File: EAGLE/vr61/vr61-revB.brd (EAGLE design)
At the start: 283.8 x 93.3 mm, 191 parts, among them M1 M25C, X1 MICROMOD-2222-C

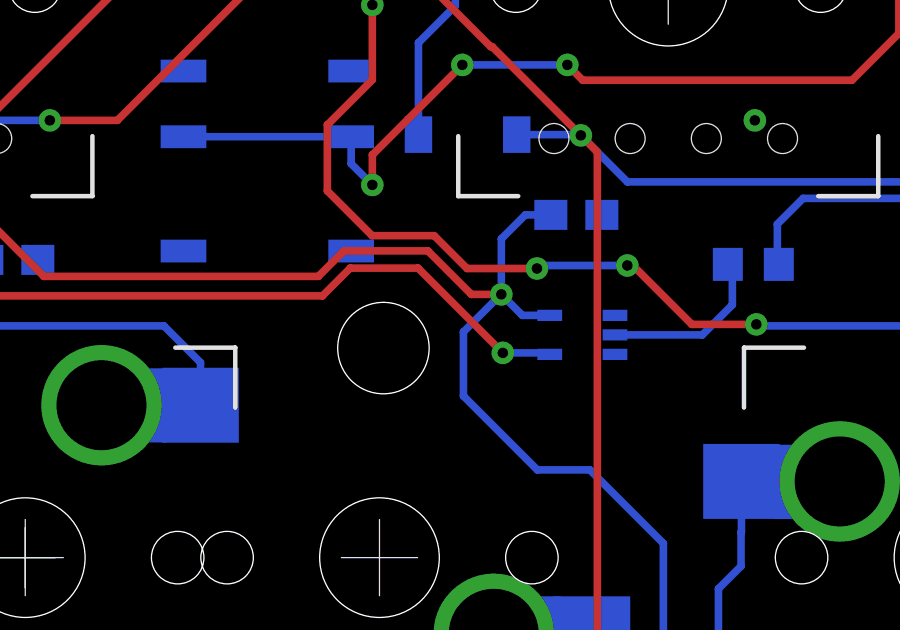
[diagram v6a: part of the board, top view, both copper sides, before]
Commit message: 74AHCT1G125GW
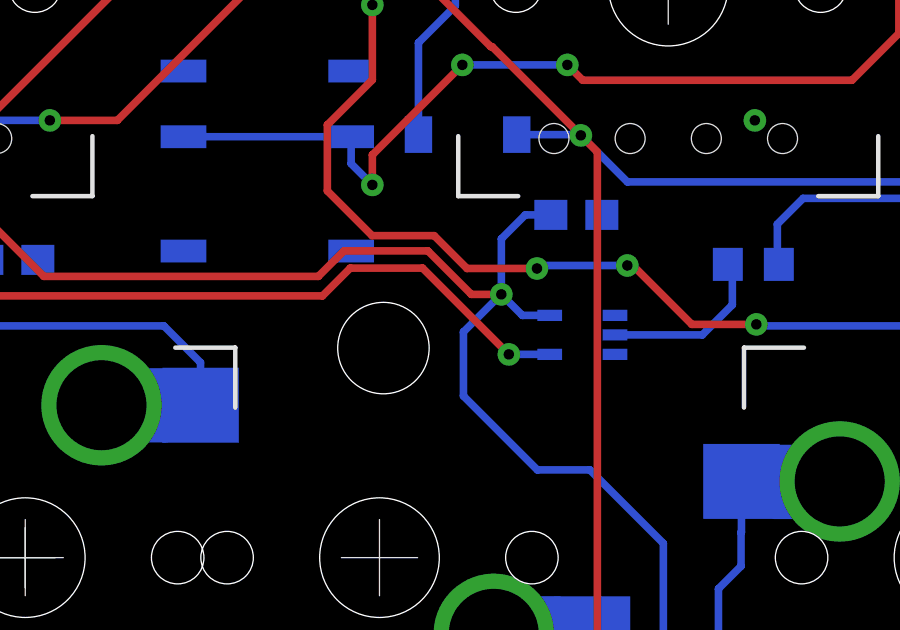
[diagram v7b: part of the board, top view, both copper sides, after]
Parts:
- U$14: value 74AHCT1G125GV -> 74AHCT1G125GW; device ts_keyboards:SC-74A -> ts_keyboards:SC-88A__TSSOP5__SOT353-1
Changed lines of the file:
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@@
 <setting verticaltext="up"/>
 </settings>
-<grid distance="1" unitdist="mm" unit="mm" style="dots" multiple="10" display="yes" altdistance="0.1" altunitdist="mm" altunit="mm"/>
+<grid distance="0.5" unitdist="mm" unit="mm" style="dots" multiple="10" display="yes" altdistance="0.05" altunitdist="mm" altunit="mm"/>
 <layers>
 <layer number="1" name="Top" color="4" fill="1" visible="yes" active="yes"/>
@@
 <element name="S_ENT2" library="ts_keyboards" package="MX-5-PIN-HOTSWAP-PAD-NS" value="MX-5-PIN-HOTSWAP-PADNO-SILK" x="273.844" y="57.15" smashed="yes"/>
 <element name="S_BSLS2" library="ts_keyboards" package="MX-5-PIN-HOTSWAP-PAD-NS" value="MX-5-PIN-HOTSWAP-PADNO-SILK" x="252.413" y="47.625" smashed="yes" rot="R180"/>
-<element name="U$14" library="ts_keyboards" package="SC-74A" value="74AHCT1G125GV" x="40" y="36" smashed="yes" rot="MR270">
-<attribute name="VALUE" x="40" y="34.095" size="0.6096" layer="28" font="vector" ratio="20" rot="MR0" align="bottom-center"/>
-</element>
 <element name="J-HOST" library="SparkFun-Connectors" library_urn="urn:adsk.eagle:library:513" package="1X02" package3d_urn="urn:adsk.eagle:package:38039/1" value="" x="90" y="40.5" smashed="yes" rot="MR90">
 <attribute name="VALUE" x="87.968" y="39.23" size="0.6096" layer="28" font="vector" ratio="20" rot="MR90"/>
@@
 <attribute name="VALUE" x="125.532" y="65.27" size="0.6096" layer="28" font="vector" ratio="20" rot="MR270"/>
 </element>
+<element name="U$14" library="ts_keyboards" package="SC-88A__TSSOP5__SOT353-1" value="74AHCT1G125GW" x="40" y="36" smashed="yes" rot="MR270">
+<attribute name="NAME" x="40" y="37.27" size="0.6096" layer="26" font="vector" ratio="20" rot="MR0" align="bottom-center"/>
+<attribute name="VALUE" x="40" y="34.095" size="0.6096" layer="28" font="vector" ratio="20" rot="MR0" align="bottom-center"/>
+</element>
 </elements>
 <signals>
@@
 <contactref element="J-UBS" pad="GND"/>
 <contactref element="J-UBS" pad="GND2"/>
-<contactref element="C07" pad="2"/>
-<contactref element="C08" pad="2"/>
-<contactref element="C09" pad="2"/>
-<contactref element="C10" pad="2"/>
-<contactref element="C11" pad="2"/>
-<contactref element="C12" pad="2"/>
 <contactref element="C13" pad="2"/>
 <contactref element="M1" pad="4"/>
 <contactref element="R8" pad="1"/>
-<contactref element="U$14" pad="3"/>
-<contactref element="U$14" pad="1"/>
 <via x="70.4" y="54.8" extent="1-16" drill="0.35"/>
 <wire x1="69.65" y1="56.225" x2="69.65" y2="55.25" width="0.254" layer="16"/>
@@
 <via x="115.5" y="89" extent="1-16" drill="0.35"/>
 <via x="71.4" y="58.5" extent="1-16" drill="0.35"/>
+<contactref element="U$14" pad="3"/>
+<contactref element="C07" pad="2"/>
+<contactref element="C08" pad="2"/>
+<contactref element="C09" pad="2"/>
+<contactref element="C10" pad="2"/>
+<contactref element="C11" pad="2"/>
+<contactref element="C12" pad="2"/>
+<contactref element="U$14" pad="1"/>
 </signal>
 <signal name="N$62">
@@
 <wire x1="28.2" y1="75.65" x2="26.55" y2="75.65" width="0.508" layer="16"/>
 <via x="28.2" y="75.65" extent="1-16" drill="0.35"/>
-<contactref element="U$14" pad="6"/>
 <wire x1="45.9012" y1="62.3114" x2="44" y2="62.3114" width="0.508" layer="16"/>
 <via x="44" y="62.3114" extent="1-16" drill="0.35"/>
@@
 <wire x1="66.21026875" y1="59.816" x2="65.32626875" y2="60.7" width="0.254" layer="16"/>
 <wire x1="58.7" y1="60.7" x2="65.32626875" y2="60.7" width="0.254" layer="16"/>
-<wire x1="38.9125" y1="36.65" x2="38" y2="36.65" width="0.254" layer="16"/>
-<wire x1="38" y1="36.65" x2="37.3" y2="37.35" width="0.254" layer="16"/>
 <via x="37.3" y="37.35" extent="1-16" drill="0.35"/>
 <wire x1="37.3" y1="37.35" x2="36.3" y2="37.35" width="0.254" layer="1"/>
@@
 <wire x1="186.85" y1="83.1" x2="186.33" y2="82.58" width="0.254" layer="16"/>
 <wire x1="186.33" y1="82.58" x2="175.62" y2="82.58" width="0.254" layer="16"/>
+<contactref element="U$14" pad="6"/>
+<wire x1="38.9125" y1="36.65" x2="38" y2="36.65" width="0.254" layer="16"/>
+<wire x1="38" y1="36.65" x2="37.3" y2="37.35" width="0.254" layer="16"/>
 </signal>
 <signal name="CC1">
@@
 <signal name="LED1ST">
 <contactref element="R6" pad="1"/>
-<contactref element="U$14" pad="2"/>
 <wire x1="44" y1="36" x2="45" y2="37" width="0.254" layer="16"/>
 <wire x1="45" y1="37" x2="45" y2="38.2" width="0.254" layer="16"/>
 <wire x1="45" y1="38.2" x2="44.85" y2="38.35" width="0.254" layer="16"/>
+<contactref element="U$14" pad="2"/>
 <wire x1="41.0875" y1="36" x2="44" y2="36" width="0.254" layer="16"/>
 </signal>
@@
 <signal name="N$66">
 <contactref element="R7" pad="2"/>
-<contactref element="U$14" pad="4"/>
 <wire x1="17.45" y1="38.5" x2="18.65" y2="37.3" width="0.254" layer="16"/>
 <wire x1="18.65" y1="37.3" x2="18.7" y2="37.3" width="0.254" layer="16"/>
 <via x="18.7" y="37.3" extent="1-16" drill="0.35"/>
-<via x="37.35" y="35.4" extent="1-16" drill="0.35"/>
+<via x="37.55" y="35.35" extent="1-16" drill="0.35"/>
 <wire x1="18.7" y1="37.3" x2="31.3372875" y2="37.3" width="0.254" layer="1"/>
 <wire x1="31.3372875" y1="37.3" x2="32.2642875" y2="38.227" width="0.254" layer="1"/>
-<wire x1="32.2642875" y1="38.227" x2="34.523" y2="38.227" width="0.254" layer="1"/>
-<wire x1="34.523" y1="38.227" x2="37.35" y2="35.4" width="0.254" layer="1"/>
-<wire x1="37.35" y1="35.4" x2="38.8625" y2="35.4" width="0.254" layer="16"/>
-<wire x1="38.8625" y1="35.4" x2="38.9125" y2="35.35" width="0.254" layer="16"/>
+<wire x1="32.2642875" y1="38.227" x2="34.673" y2="38.227" width="0.254" layer="1"/>
+<wire x1="34.673" y1="38.227" x2="37.55" y2="35.35" width="0.254" layer="1"/>
+<contactref element="U$14" pad="4"/>
+<wire x1="38.9125" y1="35.35" x2="37.55" y2="35.35" width="0.254" layer="16"/>
 </signal>
 <signal name="N$67">
